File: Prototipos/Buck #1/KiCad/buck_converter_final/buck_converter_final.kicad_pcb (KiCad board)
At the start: 2 copper layers, 100 x 100 mm, 28 parts, among them J3 Screw_Terminal_01x02, Q1 IRF9540NPBF, Q3 NPN

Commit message: Reestructuración de esquemático y PCB
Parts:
- removed C7: 2p, Capacitor_THT:C_Disc_D3.8mm_W2.6mm_P2.50mm
- removed J4: ~, Proyecto_Final:BUS_PCIE_x4_NSH
- removed R14: 180, Resistor_THT:R_Axial_DIN0207_L6.3mm_D2.5mm_P7.62mm_Horizontal
- removed REF** (x4): MountingHole_2mm, MountingHole:MountingHole_2mm
- added C4: ~, Capacitor_THT:C_Disc_D3.8mm_W2.6mm_P2.50mm, F.Cu at (124.0, 53.6)
- added D3: D_Schottky, Diode_THT:D_DO-15_P12.70mm_Horizontal, F.Cu at (119.7, 63.8)
- added J1: ~, Proyecto_final:BUS_PCIE_x4_NSH, F.Cu at (108.2, 66.5)
- added J2: Screw_Terminal_01x02, TerminalBlock_Phoenix:TerminalBlock_Phoenix_MKDS-1,5-2-5.08_1x02_P5.08mm_Horizontal, F.Cu at (149.6, 56.7)
- added K1: SANYOU_SRD_Form_C, Relay_THT:Relay_SPDT_SANYOU_SRD_Series_Form_C, F.Cu at (136.3, 72.6)
- added Q2: IRF9540NPBF, KiCad-Libraries:TO254P470X1000X2000-3P, F.Cu at (123.5, 73.5)
- added R1: 2.2k, Resistor_THT:R_Axial_DIN0207_L6.3mm_D2.5mm_P7.62mm_Horizontal, F.Cu at (118.2, 83.5)
- added R3: 100k, Resistor_THT:R_Axial_DIN0207_L6.3mm_D2.5mm_P7.62mm_Horizontal, F.Cu at (125.8, 86.3)
- added R4: 12, Resistor_THT:R_Axial_DIN0207_L6.3mm_D2.5mm_P7.62mm_Horizontal, F.Cu at (129.8, 66.7)
- added R6: ~, Resistor_THT:R_Axial_DIN0207_L6.3mm_D2.5mm_P7.62mm_Horizontal, F.Cu at (124.0, 63.8)
- C2: value 400p -> 2p
- C3: value ~ -> 400p
- D2: footprint Diode_THT:D_DO-15_P12.70mm_Horizontal -> Diode_THT:D_DO-34_SOD68_P7.62mm_Horizontal
- D4: value D_Schottky -> D_Small; footprint Diode_THT:D_DO-34_SOD68_P7.62mm_Horizontal -> Diode_THT:D_DO-41_SOD81_P7.62mm_Horizontal
- Q1: value IRF9540NPBF -> NPN; footprint KiCad-Libraries:TO254P470X1000X2000-3P -> Package_TO_SOT_THT:TO-92_Inline_Wide
- Q3: value NPN -> BC548
- R10: value 150 -> 2k2
- R11: value 2.2k -> 4k7
- R12: value 120 -> 150
- R13: value 100k -> 12k
- R2: value 12 -> 120
- R5: value ~ -> 180
- R8: value 2k2 -> 15k
- R9: value 4k7 -> 10k
- moved R7 28.9 mm to (115.4, 80.5), turned to -90 degrees
- moved D1 26.2 mm to (140.7, 89.9), turned to 180 degrees
- moved R11 22.7 mm to (135.9, 101.8), turned to 90 degrees
- moved C2 22.6 mm to (144.3, 89.2)
- moved R9 22.1 mm to (149.9, 85.6), turned to -90 degrees
- moved R12 22.0 mm to (132.8, 99.7), turned to 180 degrees
- moved R10 21.8 mm to (146.6, 96.2)
- moved D4 20.4 mm to (133.0, 68.2)
- moved C5 19.5 mm to (144.0, 63.5), turned to 90 degrees
- moved R8 19.5 mm to (115.4, 91.9)
- moved C6 19.2 mm to (132.3, 96.7), turned to 90 degrees
- moved R5 16.7 mm to (136.7, 86.3)
- moved C3 16.6 mm to (129.6, 77.4), turned to 180 degrees
- moved C1 16.5 mm to (111.3, 113.8)
- moved L1 12.8 mm to (134.1, 62.8), turned to 180 degrees
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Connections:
- net Net-(R7-Pad2) renamed IDENT_V
- C2 pad 2: Net-(D1-A) -> PGND
- C3 pad 2: PGND -> Net-(D2-A)
- C5 pad 1: Net-(J3-Pin_1) -> Net-(C5-Pad1)
- D1 pad 1: 12V -> GATE
- D1 pad 2: Net-(D1-A) -> PGND
- D2 pad 1: Net-(D1-A) -> 12V
- D2 pad 2: PGND -> Net-(D2-A)
- D4 pad 1: Gate -> 5Vdc
- D4 pad 2: PGND -> RELAY_T2
- J3 pad 1: Net-(J3-Pin_1) -> INDUCTIVE_LOAD
- L1 pad 1: Net-(D1-A) -> Net-(D2-A)
- L1 pad 2: Net-(J3-Pin_1) -> Net-(C5-Pad1)
- Q1 pad 1: Gate -> PGND
- Q1 pad 2: Net-(D1-A) -> Net-(Q1-B)
- Q1 pad 3: 12V -> GATE
- Q3 pad 1: PGND -> RELAY_T2
- Q3 pad 3: Gate -> AGND
- R10 pad 2: RETRO_MICRO -> Net-(R10-Pad2)
- R11 pad 1: PWM_CONTROL -> Net-(R10-Pad2)
- R11 pad 2: Net-(Q3-B) -> PGND
- R12 pad 1: 12V -> Net-(R10-Pad2)
- R12 pad 2: Gate -> RETRO_MICRO
- R13 pad 1: Net-(Q3-B) -> UC_RELAY
- R13 pad 2: PGND -> Net-(Q3-B)
- R2 pad 2: Net-(C2-Pad1) -> GATE
- R5 pad 1: Net-(D1-A) -> GATE
- R5 pad 2: Net-(C3-Pad1) -> Net-(C2-Pad1)
- R7 pad 1: Net-(J3-Pin_1) -> 3.3Vcc
- R8 pad 2: Net-(R10-Pad1) -> AGND
- R9 pad 1: Net-(R10-Pad1) -> Net-(C5-Pad1)
- R9 pad 2: PGND -> Net-(R10-Pad1)
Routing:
- net 12V: track 48.0 -> 12.5 mm
- net Gate: track 33.3 -> 0.00 mm
- net Net-(J3-Pin_1): track 30.6 -> 0.00 mm
- net Net-(D1-A): track 29.6 -> 0.00 mm
- net AGND: track 20.2 -> 0.00 mm
- net RETRO_MICRO: track 14.1 -> 0.00 mm
- net 5Vdc: track 0.00 -> 14.0 mm
- net RESISTIVE_LOAD: track 0.00 -> 10.3 mm
- net IDENT_V: track 8.52 -> 0.00 mm
- net Net-(Q3-B): track 7.73 -> 0.00 mm
- net PWM_CONTROL: track 7.32 -> 0.00 mm
- net Net-(R10-Pad1): track 6.90 -> 0.00 mm
- net PGND: track 1.55 -> 7.46 mm
- net Net-(C3-Pad1): track 5.52 -> 0.00 mm
- net Net-(C7-Pad1): track 3.67 -> 0.00 mm
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- removed copper zone on B.Cu, net 12V
- removed copper zone on B.Cu, net AGND
- removed copper zone on B.Cu, net Net-(D1-A)
- removed copper zone on B.Cu, net Net-(J3-Pin_1)
- removed copper zone on B.Cu, net PGND
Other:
- board size 100 x 100 mm -> 50 x 100 mm

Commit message: Avances en PCB buck
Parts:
- added REF**: MountingHole_6.4mm_M6_DIN965, MountingHole:MountingHole_6.4mm_M6_DIN965, F.Cu at (114.8, 43.0)
- added REF**: MountingHole_6.4mm_M6_DIN965, MountingHole:MountingHole_6.4mm_M6_DIN965, F.Cu at (144.8, 123.0)
- added REF**: MountingHole_6.4mm_M6_DIN965, MountingHole:MountingHole_6.4mm_M6_DIN965, F.Cu at (144.8, 43.0)
- added REF**: MountingHole_6.4mm_M6_DIN965, MountingHole:MountingHole_6.4mm_M6_DIN965, F.Cu at (114.8, 123.0)
- R7, R8: moved to B.Cu
- moved C1 31.1 mm to (136.3, 95.2), turned to 0 degrees
- moved Q3 25.6 mm to (136.3, 83.5), turned to 0 degrees
- moved D1 20.4 mm to (121.1, 84.3), turned to -90 degrees
- moved J3 20.4 mm to (149.2, 83.8)
- moved C2 17.5 mm to (127.0, 92.0), turned to 90 degrees
- moved R12 14.9 mm to (118.4, 95.8), turned to 90 degrees
- moved R5 13.1 mm to (123.8, 84.3), turned to -90 degrees
- moved R13 11.8 mm to (129.9, 87.9), turned to 0 degrees
- moved C6 11.2 mm to (121.2, 95.3), turned to 0 degrees
- moved R4 10.9 mm to (118.9, 67.2), turned to 0 degrees
- moved R2 10.8 mm to (118.8, 78.3), turned to 0 degrees
- moved C3 9.80 mm to (129.4, 67.6), turned to -90 degrees
- moved R10 9.15 mm to (138.9, 91.2)
- moved D2 8.70 mm to (118.9, 70.1), turned to 0 degrees
- moved R9 8.10 mm to (141.9, 86.8)
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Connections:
- J1 pad 10: RETRO_MICRO -> UC_RELAY
- J1 pad 11: PWM_CONTROL -> RETRO_MICRO
- J1 pad 9: UC_RELAY -> PWM_CONTROL
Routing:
- net PGND: track 7.46 -> 166.5 mm
- net AGND: track 0.00 -> 45.6 mm
- net Net-(C5-Pad1): track 0.00 -> 45.2 mm
- net 5Vdc: track 14.0 -> 51.6 mm
- net Net-(D2-A): track 0.00 -> 31.1 mm
- net RETRO_MICRO: track 0.00 -> 26.9 mm
- net UC_RELAY: track 0.00 -> 23.4 mm
- net Net-(R10-Pad2): track 0.00 -> 20.6 mm
- net GATE: track 0.00 -> 17.9 mm
- net IDENT_V: track 0.00 -> 13.7 mm
- net RELAY_T2: track 0.00 -> 12.2 mm
- net PWM_CONTROL: track 0.00 -> 11.0 mm
- net Net-(Q1-B): track 0.00 -> 9.37 mm
- net 3.3Vcc: track 0.00 -> 7.00 mm
- net INDUCTIVE_LOAD: track 0.00 -> 5.69 mm
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- added copper zone on B.Cu, net 12V
- added copper zone on B.Cu, net 5Vdc
- added copper zone on B.Cu, net INDUCTIVE_LOAD
- added copper zone on B.Cu, net Net-(C5-Pad1)
- added copper zone on B.Cu, net Net-(D2-A)
- added copper zone on B.Cu, net PGND
- added copper zone on B.Cu, net RESISTIVE_LOAD
- added copper zone on B.Cu, net UC_RELAY

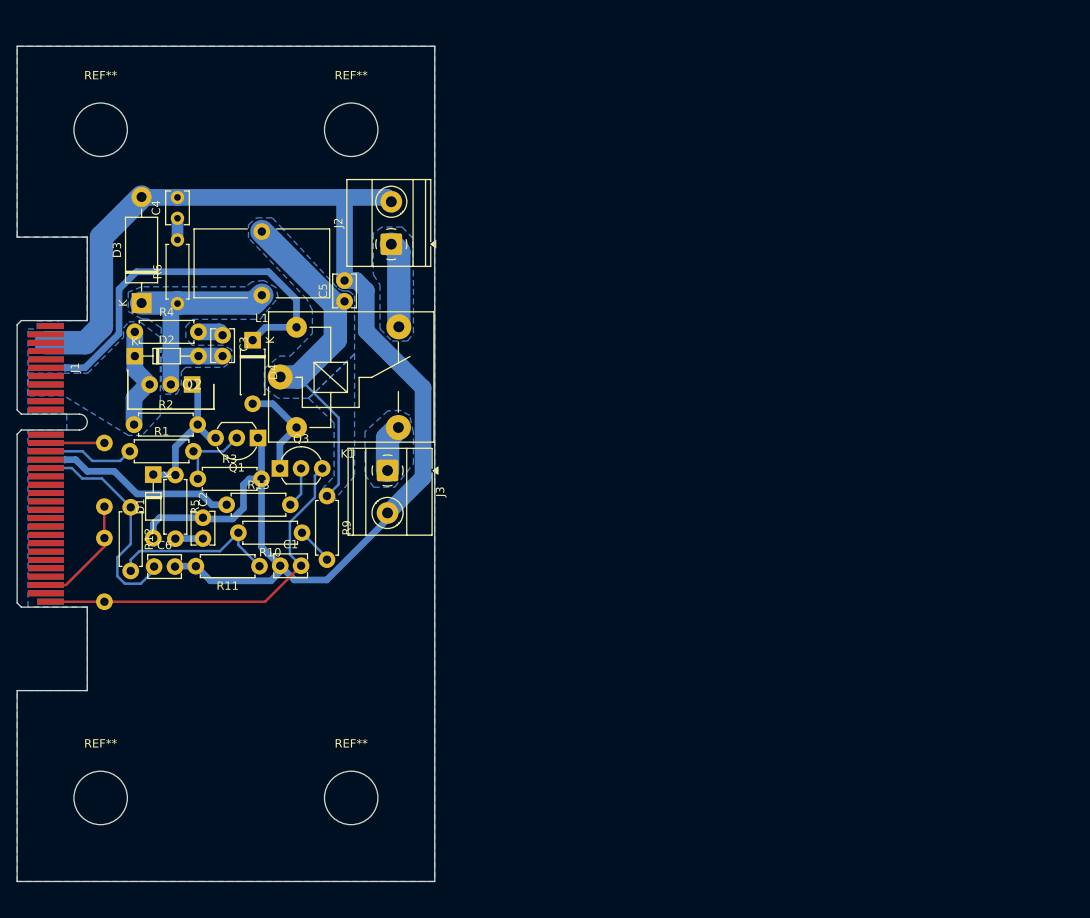
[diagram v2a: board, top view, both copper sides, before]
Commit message: Avances en PCB, etiqueta de bloques
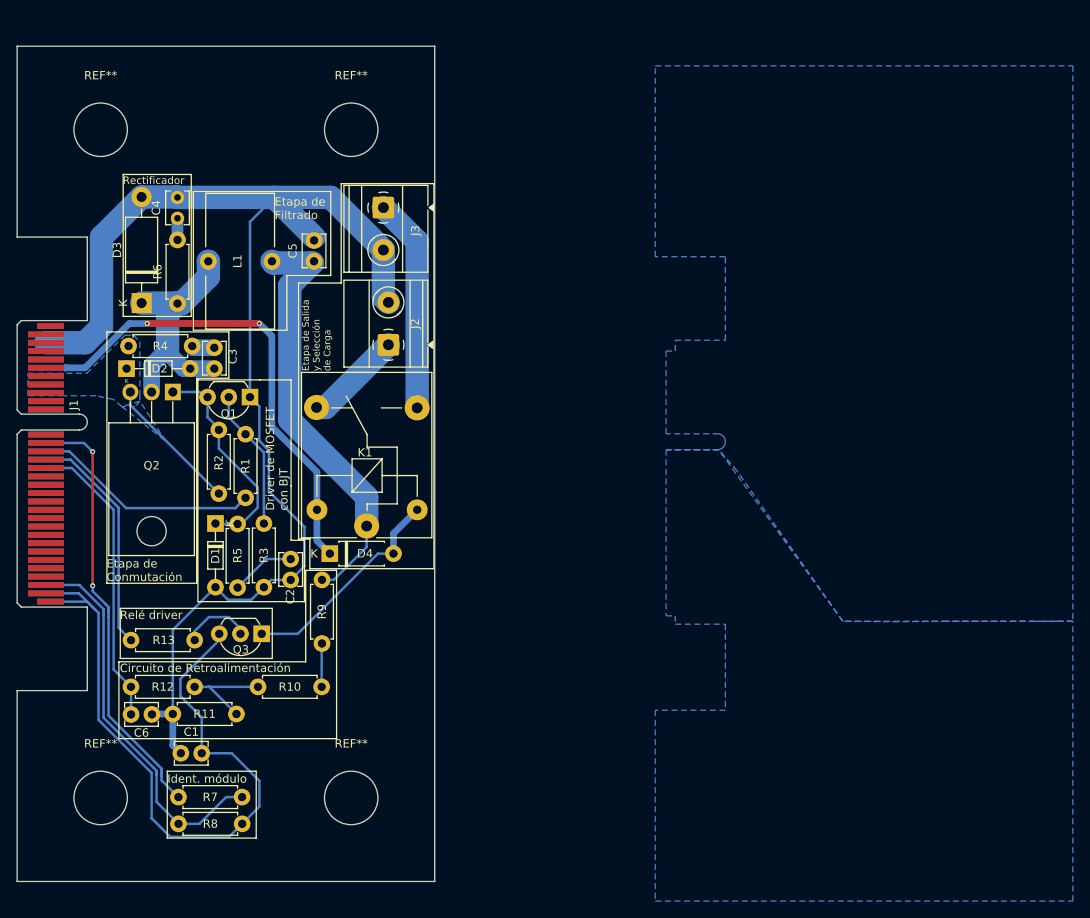
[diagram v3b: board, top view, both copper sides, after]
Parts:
- Q2: footprint KiCad-Libraries:TO254P470X1000X2000-3P -> Package_TO_SOT_THT:TO-220-3_Horizontal_TabDown
- R7, R8: moved to F.Cu
- moved R7 43.3 mm to (124.1, 122.9), turned to 0 degrees
- moved R8 35.3 mm to (124.1, 126.1), turned to 0 degrees
- moved J3 31.5 mm to (148.7, 52.3)
- moved D4 27.2 mm to (142.2, 93.8), turned to 0 degrees
- moved C1 25.4 mm to (124.4, 117.7)
- moved K1 20.6 mm to (146.7, 90.5), turned to 90 degrees
- moved Q3 19.9 mm to (134.1, 103.3), turned to 180 degrees
- moved R13 19.8 mm to (118.4, 104.1)
- moved R10 18.6 mm to (141.3, 109.7)
- moved C6 17.9 mm to (118.4, 113.0)
- moved R11 17.9 mm to (131.1, 113.0)
- moved R12 15.8 mm to (126.0, 109.7), turned to 180 degrees
- moved R1 14.9 mm to (132.2, 87.1), turned to 90 degrees
- moved R2 13.1 mm to (128.9, 86.6), turned to 90 degrees
- moved J2 12.1 mm to (149.2, 68.8)
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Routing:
- net 3.3Vcc: track 7.00 -> 51.6 mm, vias 0 -> 2
- net AGND: track 45.6 -> 84.2 mm
- net IDENT_V: track 13.7 -> 46.5 mm
- net INDUCTIVE_LOAD: track 5.69 -> 25.7 mm
- net PWM_CONTROL: track 11.0 -> 27.2 mm
- net RELAY_T2: track 12.2 -> 26.2 mm
- net PGND: track 166.5 -> 155.8 mm
- net RETRO_MICRO: track 26.9 -> 35.5 mm
- net Net-(Q1-B): track 9.37 -> 17.8 mm
- net Net-(R10-Pad2): track 20.6 -> 12.2 mm
- net GATE: track 17.9 -> 26.0 mm
- net 5Vdc: track 51.6 -> 59.0 mm, vias 0 -> 2
- net Net-(C5-Pad1): track 45.2 -> 50.8 mm
- net Net-(C2-Pad1): track 3.30 -> 7.93 mm
- net UC_RELAY: track 23.4 -> 27.6 mm
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- added copper zone on B.Cu, net AGND
- removed copper zone on B.Cu, net INDUCTIVE_LOAD
- removed copper zone on B.Cu, net Net-(C5-Pad1)
- removed copper zone on B.Cu, net Net-(D2-A)
- removed copper zone on B.Cu, net RESISTIVE_LOAD
- removed copper zone on B.Cu, net UC_RELAY
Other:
- board text added: "Circuito de Retroalimentación"
- board text added: "Driver de MOSFET con BJT"
- board text added: "Etapa de Conmutación"
- board text added: "Etapa de Filtrado"
- board text added: "Etapa de Salida y Selección de Carga"
- board text added: "Ident. módulo"
- board text added: "Rectificador"
- board text added: "Relé driver"

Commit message: PCB final, versión preliminar, con testpoints
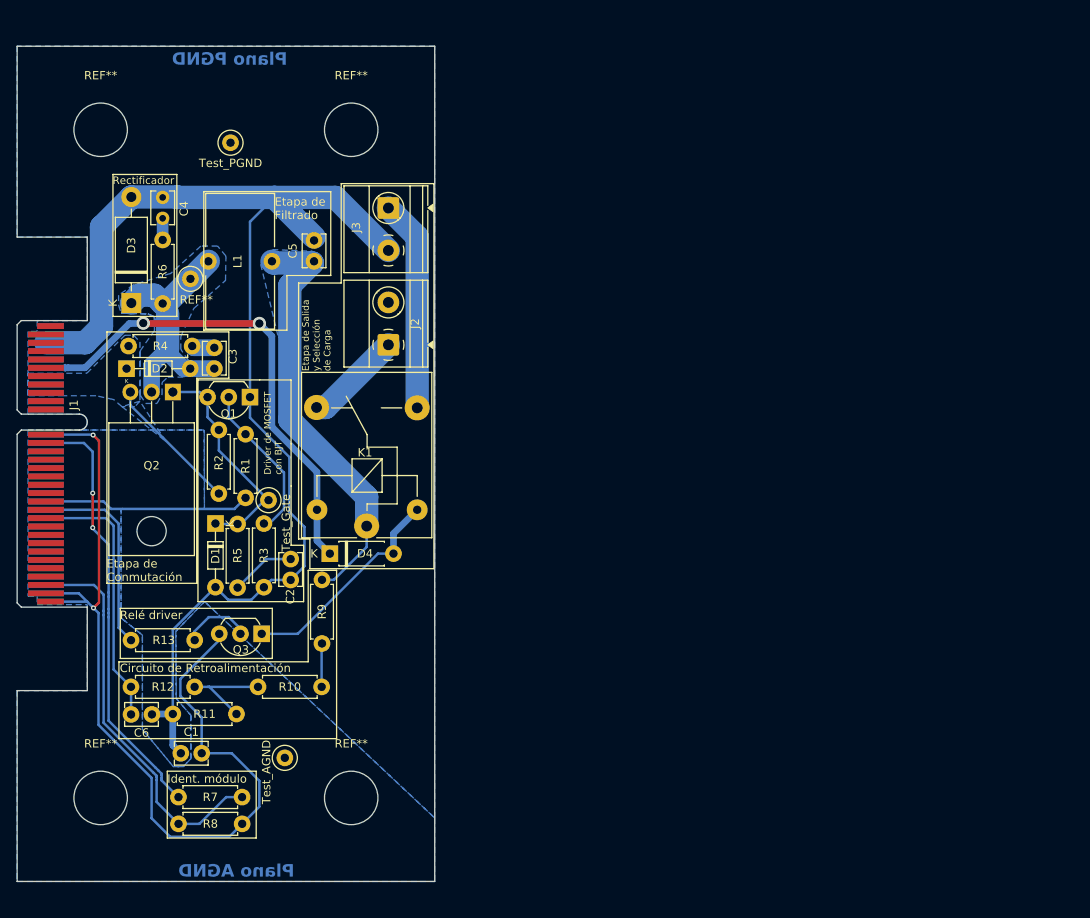
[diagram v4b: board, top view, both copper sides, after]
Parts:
- added REF**: TestPoint_Loop_D1.80mm_Drill1.0mm_Beaded, TestPoint:TestPoint_Loop_D1.80mm_Drill1.0mm_Beaded, F.Cu at (125.5, 60.9)
- added Test_AGND: TestPoint_Loop_D1.80mm_Drill1.0mm_Beaded, TestPoint:TestPoint_Loop_D1.80mm_Drill1.0mm_Beaded, F.Cu at (136.8, 118.2)
- added Test_Gate: TestPoint_Loop_D1.80mm_Drill1.0mm_Beaded, TestPoint:TestPoint_Loop_D1.80mm_Drill1.0mm_Beaded, F.Cu at (134.9, 87.3)
- added Test_PGND: TestPoint_Loop_D1.80mm_Drill1.0mm_Beaded, TestPoint:TestPoint_Loop_D1.80mm_Drill1.0mm_Beaded, F.Cu at (130.3, 44.5)
- moved J3 5.16 mm to (149.2, 57.5), turned to 90 degrees
- moved C4 1.78 mm to (122.2, 53.6)
- moved R6 1.78 mm to (122.2, 63.8)
- moved D3 1.23 mm to (118.5, 63.8)
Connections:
- J1 pad 10: UC_RELAY -> unconnected-(J1-S2-Pad10)
- J1 pad 11: RETRO_MICRO -> unconnected-(J1-S3-Pad11)
- J1 pad 15: unconnected-(J1-S7-Pad15) -> PWM_CONTROL
- J1 pad 16: unconnected-(J1-S8-Pad16) -> UC_RELAY
- J1 pad 17: unconnected-(J1-S9-Pad17) -> RETRO_MICRO
- J1 pad 9: PWM_CONTROL -> unconnected-(J1-S1-Pad9)
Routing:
- net AGND: track 84.2 -> 109.8 mm, vias 0 -> 2
- net PGND: track 155.8 -> 150.6 mm
- net UC_RELAY: track 27.6 -> 24.0 mm
- net RETRO_MICRO: track 35.5 -> 31.9 mm
- net PWM_CONTROL: track 27.2 -> 24.8 mm
- net Net-(Q1-B): track 17.8 -> 20.2 mm
- net GATE: track 26.0 -> 27.3 mm
- net IDENT_V: track 46.5 -> 47.5 mm
- net Net-(D2-A): track 29.9 -> 29.1 mm
- added copper zone on B.Cu, net Net-(C5-Pad1)
- added copper zone on B.Cu, net Net-(D2-A)
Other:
- board text added: "Plano AGND"
- board text added: "Plano PGND"

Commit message: Avances PCB
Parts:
- removed the REF** at (144.8, 123.0)
- removed the REF** at (144.8, 43.0)
- removed Test_AGND, Test_PGND: TestPoint_Loop_D1.80mm_Drill1.0mm_Beaded, TestPoint:TestPoint_Loop_D1.80mm_Drill1.0mm_Beaded
- moved REF** 8.49 mm to (108.8, 37.0)
- moved REF** 8.49 mm to (108.8, 129.0)
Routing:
- net AGND: track 109.8 -> 110.9 mm

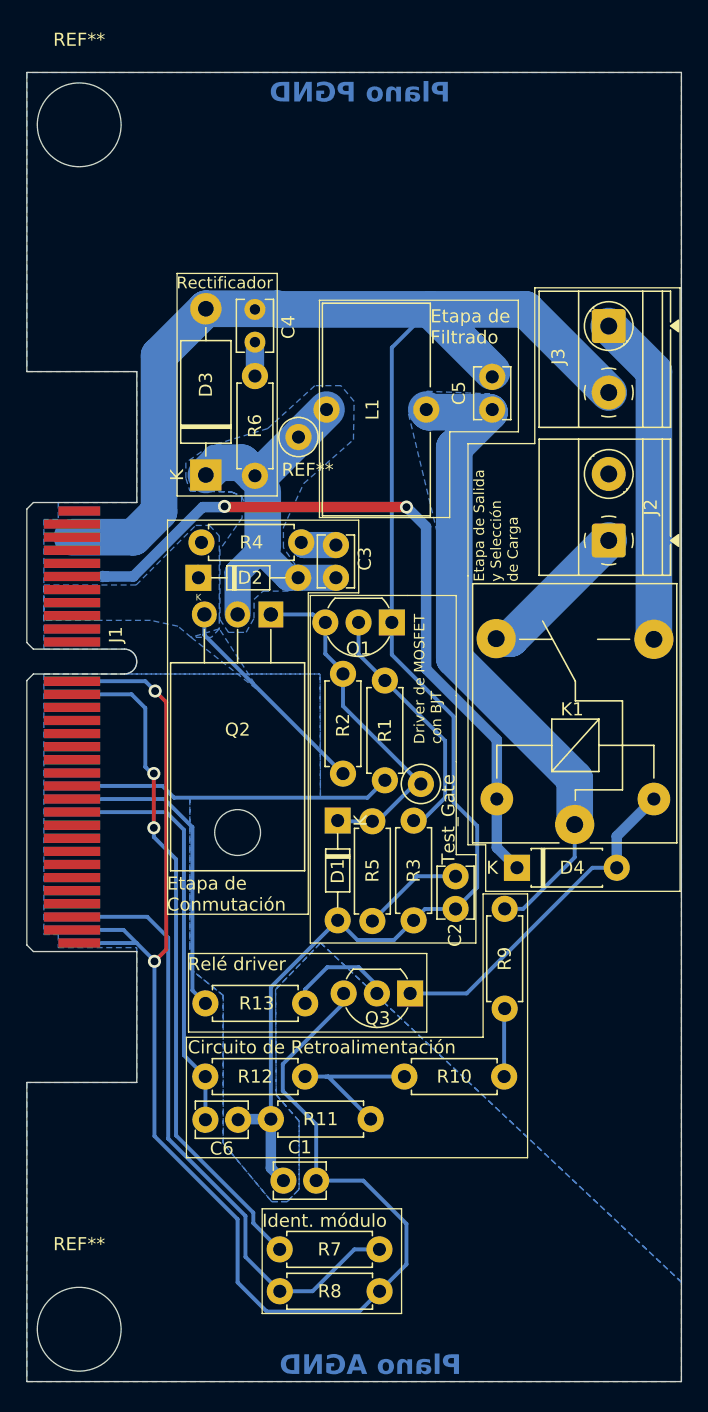
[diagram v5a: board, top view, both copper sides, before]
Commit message: PCB Buck versión 1.0 finalizada
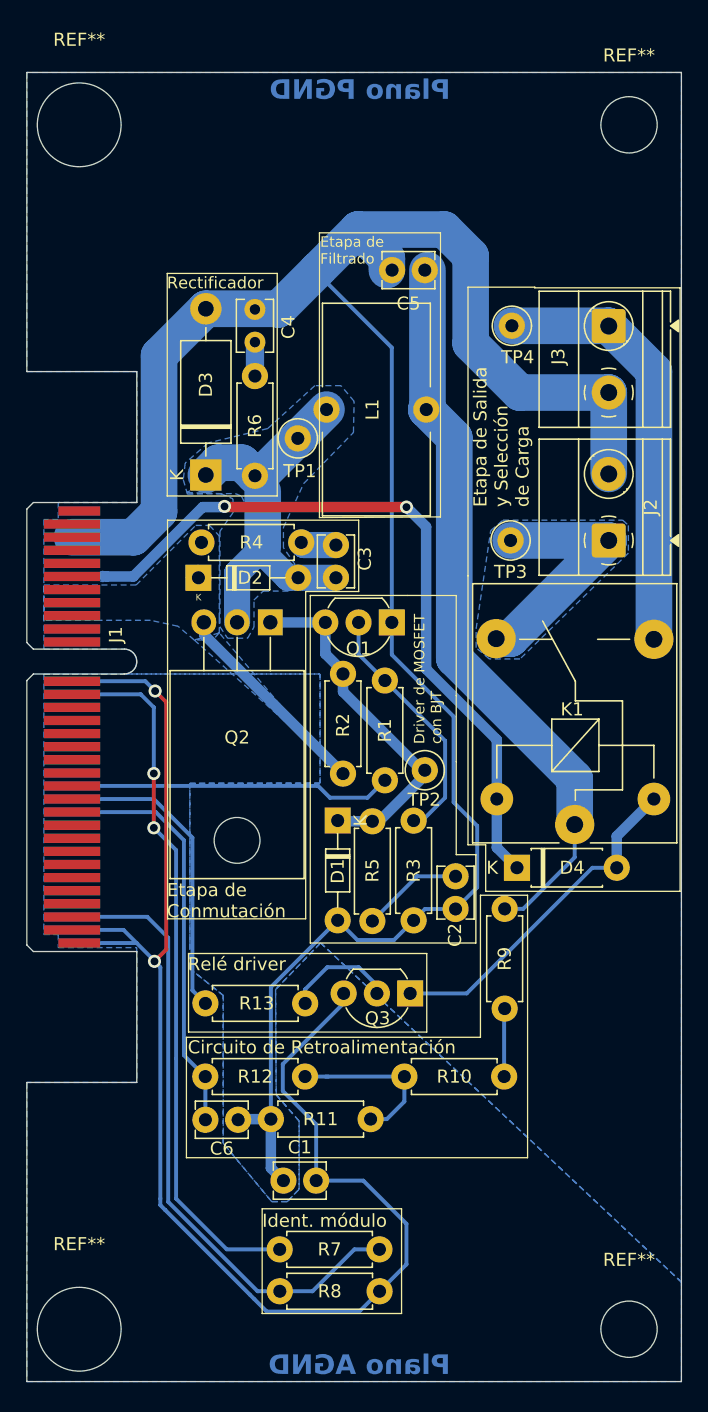
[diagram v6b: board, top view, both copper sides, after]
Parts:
- removed the REF** at (125.5, 60.9)
- removed Test_Gate: TestPoint_Loop_D1.80mm_Drill1.0mm_Beaded, TestPoint:TestPoint_Loop_D1.80mm_Drill1.0mm_Beaded
- added REF**: MountingHole_4.3mm_M4, MountingHole:MountingHole_4.3mm_M4, F.Cu at (150.8, 37.0)
- added REF**: MountingHole_4.3mm_M4, MountingHole:MountingHole_4.3mm_M4, F.Cu at (150.8, 129.0)
- added TP1: DRAIN, TestPoint:TestPoint_Loop_D1.80mm_Drill1.0mm_Beaded, F.Cu at (125.5, 61.0)
- added TP2: GATE, TestPoint:TestPoint_Loop_D1.80mm_Drill1.0mm_Beaded, F.Cu at (135.2, 86.3)
- added TP3: LOAD_1, TestPoint:TestPoint_Loop_D1.80mm_Drill1.0mm_Beaded, F.Cu at (141.8, 68.8)
- added TP4: LOAD_2, TestPoint:TestPoint_Loop_D1.80mm_Drill1.0mm_Beaded, F.Cu at (141.8, 52.4)
- moved C5 11.8 mm to (135.2, 48.1), turned to 180 degrees
- moved Q2 0.60 mm to (123.4, 75.0)
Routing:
- net PGND: track 150.6 -> 167.2 mm
- net RESISTIVE_LOAD: track 11.7 -> 19.2 mm
- net INDUCTIVE_LOAD: track 25.4 -> 32.8 mm
- net Net-(C5-Pad1): track 50.8 -> 56.6 mm
- net 3.3Vcc: track 51.7 -> 54.4 mm
- net IDENT_V: track 47.5 -> 48.5 mm
- net Net-(D2-A): track 29.1 -> 29.7 mm
- net 12V: track 16.6 -> 16.0 mm
- added copper zone on B.Cu, net RESISTIVE_LOAD
- removed copper zone on B.Cu, net Net-(C5-Pad1)
